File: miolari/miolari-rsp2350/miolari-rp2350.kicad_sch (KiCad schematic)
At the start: 67 parts, among them CN1 XT60PW-M, J2 USB2UART, J3 lcd jumper, J4 lcd jumper, J5 lcd jumper, J6 1.47 IPS LCD, J7 ConnBattery, J8 MainConnector, SW3 BOOT SELECTOR, SW4 RST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

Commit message: miolari rp2350a routing phase2
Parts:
- L2: footprint Inductor_SMD:L_0805_2012Metric_Pad1.15x1.40mm_HandSolder -> Inductor_SMD:L_0805_2012Metric_Pad1.05x1.20mm_HandSolder
- U5: footprint Package_SO:SOIC-8_5.23x5.23mm_P1.27mm -> Package_SO:SOIC-8_5.3x5.3mm_P1.27mm
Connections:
- net BLK is gone; now on net GPIO15: J5.8 (Pin_8), J6.8 (Pin_8)
- net CS is gone; now on net GPIO14: J5.7 (Pin_7), J6.7 (Pin_7)
- net DC is gone; now on net GPIO13: J5.6 (Pin_6), J6.6 (Pin_6)
- net MOSI is gone; now on net GPIO11: J5.4 (Pin_4), J6.4 (Pin_4)
- net RESET is gone; now on net GPIO12: J5.5 (Pin_5), J6.5 (Pin_5)
- net SCK is gone; now on net GPIO10: J5.3 (Pin_3), J6.3 (Pin_3)
- net +12V: now also J8.39 (Pin_39); no longer J8.40 (Pin_40)
- net +3.3V: now also J8.35 (Pin_35); no longer J8.36 (Pin_36)
- net GND: now also J8.40 (Pin_40); no longer J8.39 (Pin_39)
- net GPIO0: now also J8.38 (Pin_38); no longer J8.1 (Pin_1)
- net GPIO1: now also J8.36 (Pin_36); no longer J8.3 (Pin_3)
- net GPIO10: now also J8.18 (Pin_18); no longer J8.21 (Pin_21)
- net GPIO11: now also J8.16 (Pin_16); no longer J8.23 (Pin_23)
- net GPIO12: now also J8.14 (Pin_14); no longer J8.25 (Pin_25)
- net GPIO13: now also J8.12 (Pin_12); no longer J8.27 (Pin_27)
- net GPIO14: now also J8.10 (Pin_10); no longer J8.29 (Pin_29)
- net GPIO15: now also J8.8 (Pin_8); no longer J8.31 (Pin_31)
- net GPIO16: now also J8.6 (Pin_6); no longer J8.33 (Pin_33)
- net GPIO17: now also J8.4 (Pin_4); no longer J8.35 (Pin_35)
- net GPIO18: now also J8.2 (Pin_2); no longer J8.37 (Pin_37)
- net GPIO19: now also J8.1 (Pin_1); no longer J8.2 (Pin_2)
- net GPIO2: now also J8.34 (Pin_34); no longer J8.5 (Pin_5)
- net GPIO20: now also J8.3 (Pin_3); no longer J8.4 (Pin_4)
- net GPIO21: now also J8.5 (Pin_5); no longer J8.6 (Pin_6)
- net GPIO22: now also J8.7 (Pin_7); no longer J8.8 (Pin_8)
- net GPIO23: now also J8.9 (Pin_9); no longer J8.10 (Pin_10)
- net GPIO24: now also J8.11 (Pin_11); no longer J8.12 (Pin_12)
- net GPIO25: now also J8.13 (Pin_13); no longer J8.14 (Pin_14)
- net GPIO26_ADC0: now also J8.15 (Pin_15); no longer J8.16 (Pin_16)
- net GPIO27_ADC1: now also J8.17 (Pin_17); no longer J8.18 (Pin_18)
- net GPIO28_ADC2: now also J8.19 (Pin_19); no longer J8.20 (Pin_20)
- net GPIO29_ADC3: now also J8.21 (Pin_21); no longer J8.22 (Pin_22)
- net GPIO3: now also J8.32 (Pin_32); no longer J8.7 (Pin_7)
- net GPIO4: now also J8.30 (Pin_30); no longer J8.9 (Pin_9)
- net GPIO5: now also J8.28 (Pin_28); no longer J8.11 (Pin_11)
- net GPIO6: now also J8.26 (Pin_26); no longer J8.13 (Pin_13)
- net GPIO7: now also J8.24 (Pin_24); no longer J8.15 (Pin_15)
- net GPIO8: now also J8.22 (Pin_22); no longer J8.17 (Pin_17)
- net GPIO9: now also J8.20 (Pin_20); no longer J8.19 (Pin_19)
- net SWCLK: now also J8.23 (Pin_23); no longer J8.24 (Pin_24)
- net SWD: now also J8.25 (Pin_25); no longer J8.26 (Pin_26)
- net USB_DM: now also R7.1; no longer R8.1
- net USB_DP: now also R8.1; no longer R7.1
- net VBUS: now also J8.37 (Pin_37); no longer J8.38 (Pin_38)

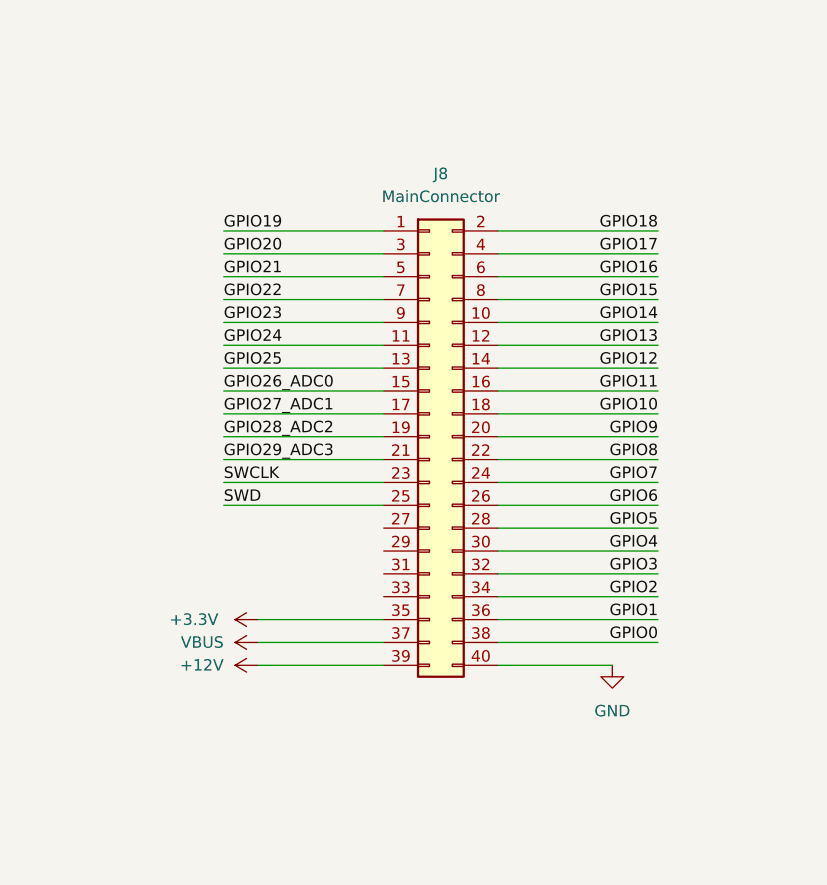
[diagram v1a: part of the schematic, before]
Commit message: add idc connector to miolari tmc2209
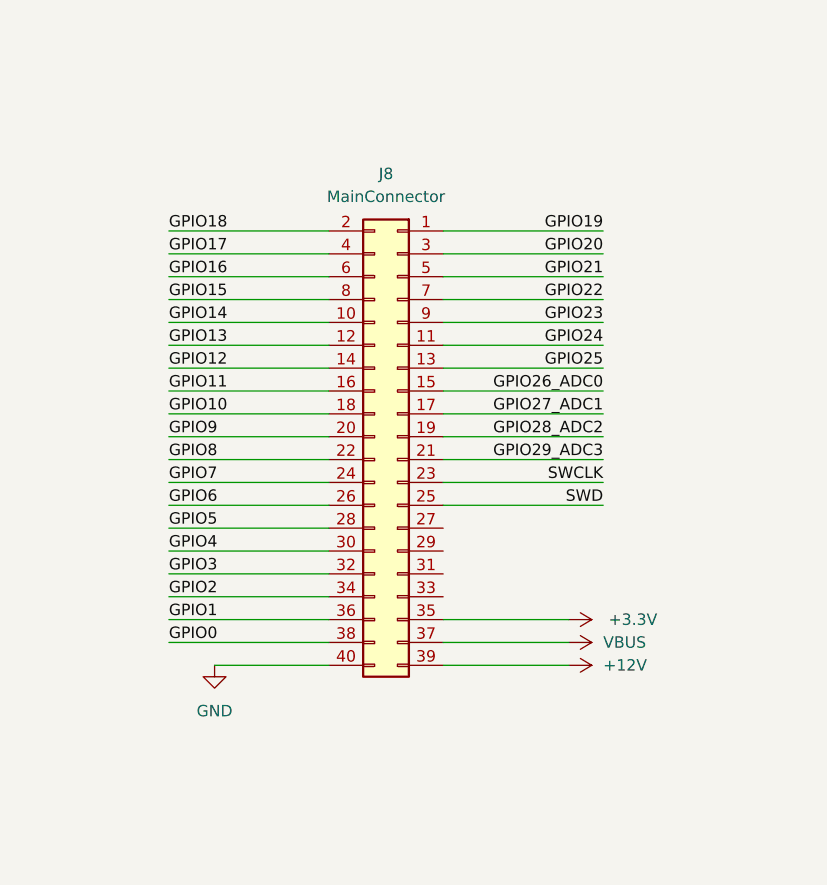
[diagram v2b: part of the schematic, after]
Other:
- moved on the sheet: J8
